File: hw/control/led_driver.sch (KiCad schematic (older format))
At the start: 0 parts

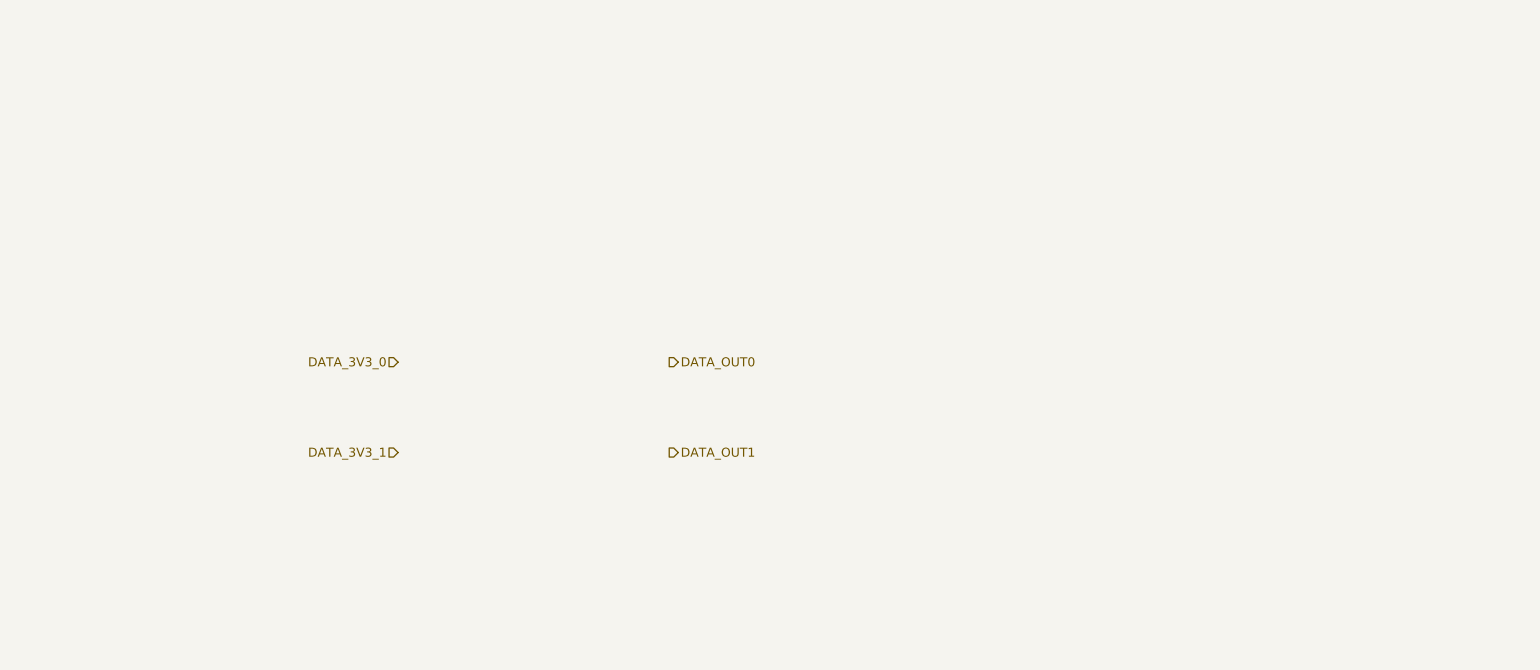
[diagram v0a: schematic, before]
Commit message: [hw] Add LED bus driver
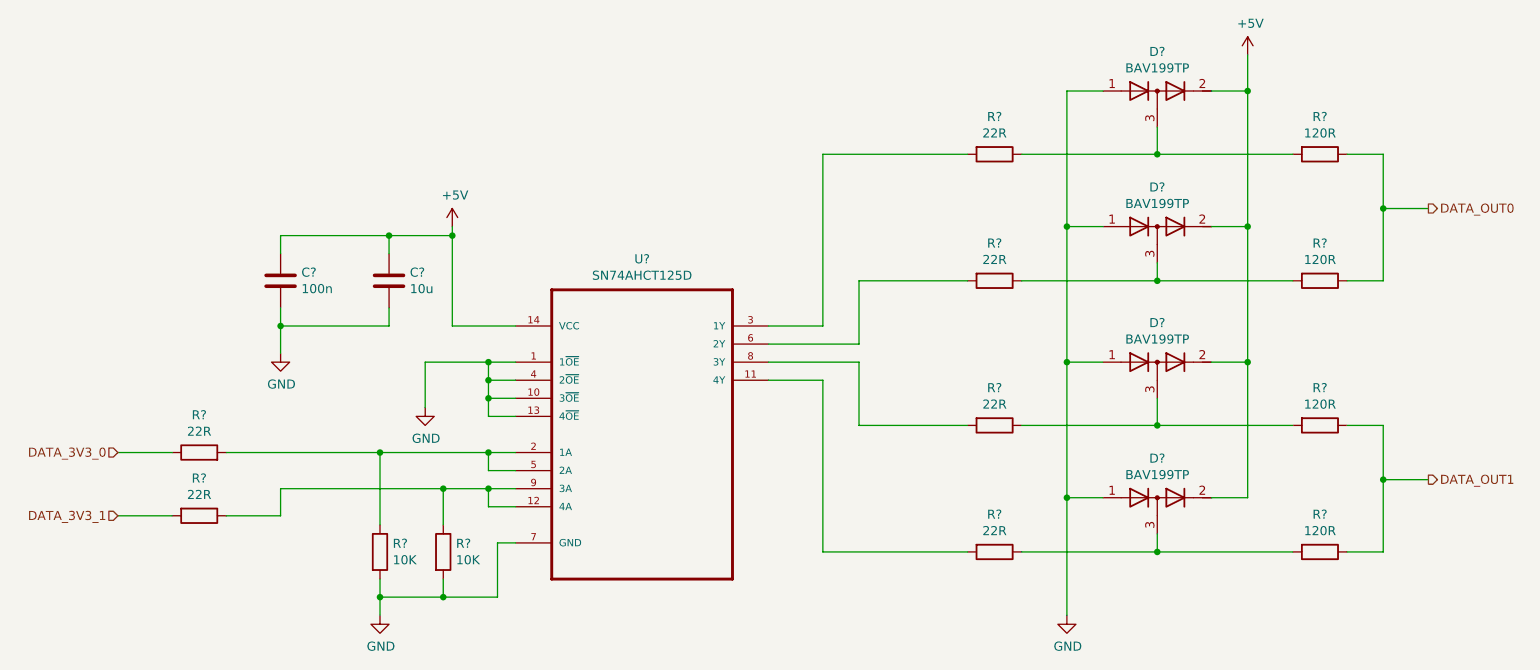
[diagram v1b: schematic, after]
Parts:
- added C?: 10u, symbol Device:C
- added C?: 100n, symbol Device:C
- added D? (x4): BAV199TP, Package_TO_SOT_SMD:SOT-23, symbol my:BAV199TP
- added R? (x2): 10K, symbol Device:R
- added R? (x6): 22R, symbol Device:R
- added R? (x4): 120R, symbol Device:R
- added U?: SN74AHCT125D, SOIC127P600X175-14N, symbol SN74AHCT125D:SN74AHCT125D
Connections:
- net DATA_3V3_0: now also R?.1
- net DATA_3V3_1: now also R?.2
- net DATA_OUT0: now also R?.1, R?.1
- net DATA_OUT1: now also R?.1, R?.1
- new net: R?.2, U?.11 (4Y)
- new net: R?.1, R?.1, U?.12 (4A), U?.9 (3A)
- new net: R?.1, R?.2, U?.2 (1A), U?.5 (2A)
- new net: R?.2, U?.3 (1Y)
- new net: R?.2, U?.6 (2Y)
- new net: R?.2, U?.8 (3Y)
- new net: D?.3 (K3), R?.1, R?.2 (x4)
- new net +5V: C?.1, C?.1, D?.2 (K2), D?.2 (K2), D?.2 (K2), D?.2 (K2), U?.14 (VCC)
- new net GND: C?.2, C?.2, D?.1 (A1), D?.1 (A1), D?.1 (A1), D?.1 (A1), R?.2, R?.2, U?.1 (1~OE), U?.10 (3~OE), U?.13 (4~OE), U?.4 (2~OE), U?.7 (GND)

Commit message: [hw] Add annotations, minor fixes
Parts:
- R707, R708: renamed from R?; value 22R -> 33R
- gave numbers to parts that had none: 17
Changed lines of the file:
@@
 encoding utf-8
 Sheet 7 7
-Title ""
-Date ""
-Rev ""
-Comp ""
-Comment1 ""
+Title "WS2812 Controller"
+Date "2021-09-16"
+Rev "1"
+Comp "Stefan Misik"
+Comment1 "LED Data Driver"
 Comment2 ""
 Comment3 ""
@@
 DATA_OUT1
 $Comp
-L SN74AHCT125D:SN74AHCT125D U?
+L SN74AHCT125D:SN74AHCT125D U701
 U 1 1 6146F060
 P 4850 4300
-F 0 "U?" H 4850 5170 50  0000 C CNN
+F 0 "U701" H 4850 5170 50  0000 C CNN
 F 1 "SN74AHCT125D" H 4850 5079 50  0000 C CNN
 F 2 "SOIC127P600X175-14N" H 4850 4300 50  0001 L BNN
@@
 	4000 4700 4150 4700
 $Comp
-L power:+5V #PWR?
+L power:+5V #PWR0702
 U 1 1 61473D10
 P 3800 3250
-F 0 "#PWR?" H 3800 3100 50  0001 C CNN
+F 0 "#PWR0702" H 3800 3100 50  0001 C CNN
 F 1 "+5V" H 3815 3423 50  0000 C CNN
 F 2 "" H 3800 3250 50  0001 C CNN
@@
 	3800 3800 4150 3800
 $Comp
-L Device:C C?
+L Device:C C702
 U 1 1 6147522C
 P 3450 3550
-F 0 "C?" H 3565 3596 50  0000 L CNN
+F 0 "C702" H 3565 3596 50  0000 L CNN
 F 1 "10u" H 3565 3505 50  0000 L CNN
 F 2 "" H 3488 3400 50  0001 C CNN
@@
 $EndComp
 $Comp
-L Device:C C?
+L Device:C C701
 U 1 1 61475C06
 P 2850 3550
-F 0 "C?" H 2965 3596 50  0000 L CNN
+F 0 "C701" H 2965 3596 50  0000 L CNN
 F 1 "100n" H 2965 3505 50  0000 L CNN
 F 2 "" H 2888 3400 50  0001 C CNN
@@
 	3450 3300 3800 3300
 $Comp
-L power:GND #PWR?
+L power:GND #PWR0703
 U 1 1 61476844
 P 2850 3950
-F 0 "#PWR?" H 2850 3700 50  0001 C CNN
+F 0 "#PWR0703" H 2850 3700 50  0001 C CNN
 F 1 "GND" H 2855 3777 50  0000 C CNN
 F 2 "" H 2850 3950 50  0001 C CNN
@@
 	2850 3800 2850 3700
 $Comp
-L Device:R R?
+L Device:R R710
 U 1 1 6147BD41
 P 3750 5050
-F 0 "R?" H 3820 5096 50  0000 L CNN
+F 0 "R710" H 3820 5096 50  0000 L CNN
 F 1 "10K" H 3820 5005 50  0000 L CNN
 F 2 "" V 3680 5050 50  0001 C CNN
@@
 $EndComp
 $Comp
-L Device:R R?
+L Device:R R709
 U 1 1 6147C52A
 P 3400 5050
-F 0 "R?" H 3470 5096 50  0000 L CNN
+F 0 "R709" H 3470 5096 50  0000 L CNN
 F 1 "10K" H 3470 5005 50  0000 L CNN
 F 2 "" V 3330 5050 50  0001 C CNN
@@
 	3400 4900 3400 4500
 $Comp
-L power:GND #PWR?
+L power:GND #PWR0705
 U 1 1 6147D2D2
 P 3400 5400
-F 0 "#PWR?" H 3400 5150 50  0001 C CNN
+F 0 "#PWR0705" H 3400 5150 50  0001 C CNN
 F 1 "GND" H 3405 5227 50  0000 C CNN
 F 2 "" H 3400 5400 50  0001 C CNN
@@
 Connection ~ 3750 5300
 $Comp
-L power:GND #PWR?
+L power:GND #PWR0704
 U 1 1 614804D8
 P 3650 4250
-F 0 "#PWR?" H 3650 4000 50  0001 C CNN
+F 0 "#PWR0704" H 3650 4000 50  0001 C CNN
 F 1 "GND" H 3655 4077 50  0000 C CNN
 F 2 "" H 3650 4250 50  0001 C CNN
@@
 Connection ~ 4000 4200
 $Comp
-L Device:R R?
+L Device:R R701
 U 1 1 61482CAE
 P 6800 2850
-F 0 "R?" V 6593 2850 50  0000 C CNN
+F 0 "R701" V 6593 2850 50  0000 C CNN
 F 1 "22R" V 6684 2850 50  0000 C CNN
 F 2 "" V 6730 2850 50  0001 C CNN
@@
 $EndComp
 $Comp
-L Device:R R?
+L Device:R R702
 U 1 1 614835EC
 P 8600 2850
-F 0 "R?" V 8393 2850 50  0000 C CNN
+F 0 "R702" V 8393 2850 50  0000 C CNN
 F 1 "120R" V 8484 2850 50  0000 C CNN
 F 2 "" V 8530 2850 50  0001 C CNN
@@
 $EndComp
 $Comp
-L Device:R R?
+L Device:R R703
 U 1 1 61483CB0
 P 6800 3550
-F 0 "R?" V 6593 3550 50  0000 C CNN
+F 0 "R703" V 6593 3550 50  0000 C CNN
 F 1 "22R" V 6684 3550 50  0000 C CNN
 F 2 "" V 6730 3550 50  0001 C CNN
@@
 $EndComp
 $Comp
-L Device:R R?
+L Device:R R704
 U 1 1 61484724
 P 8600 3550
-F 0 "R?" V 8393 3550 50  0000 C CNN
+F 0 "R704" V 8393 3550 50  0000 C CNN
 F 1 "120R" V 8484 3550 50  0000 C CNN
 F 2 "" V 8530 3550 50  0001 C CNN
@@
 $EndComp
 $Comp
-L my:BAV199TP D?
+L my:BAV199TP D701
 U 1 1 6149355D
 P 7700 2500
-F 0 "D?" H 7700 2717 50  0000 C CNN
+F 0 "D701" H 7700 2717 50  0000 C CNN
 F 1 "BAV199TP" H 7700 2626 50  0000 C CNN
 F 2 "Package_TO_SOT_SMD:SOT-23" H 7700 2000 50  0001 C CNN
@@
 $EndComp
 $Comp
-L my:BAV199TP D?
+L my:BAV199TP D702
 U 1 1 61495B2C
 P 7700 3250
-F 0 "D?" H 7700 3467 50  0000 C CNN
+F 0 "D702" H 7700 3467 50  0000 C CNN
 F 1 "BAV199TP" H 7700 3376 50  0000 C CNN
 F 2 "Package_TO_SOT_SMD:SOT-23" H 7700 2750 50  0001 C CNN
@@
 	8950 2850 8750 2850
 $Comp
-L Device:R R?
+L Device:R R705
 U 1 1 614B3F72
 P 6800 4350
-F 0 "R?" V 6593 4350 50  0000 C CNN
+F 0 "R705" V 6593 4350 50  0000 C CNN
 F 1 "22R" V 6684 4350 50  0000 C CNN
 F 2 "" V 6730 4350 50  0001 C CNN
@@
 $EndComp
 $Comp
-L Device:R R?
+L Device:R R706
 U 1 1 614B3F78
 P 8600 4350
-F 0 "R?" V 8393 4350 50  0000 C CNN
+F 0 "R706" V 8393 4350 50  0000 C CNN
 F 1 "120R" V 8484 4350 50  0000 C CNN
 F 2 "" V 8530 4350 50  0001 C CNN
@@
 $EndComp
 $Comp
-L Device:R R?
+L Device:R R711
 U 1 1 614B3F7E
 P 6800 5050
-F 0 "R?" V 6593 5050 50  0000 C CNN
+F 0 "R711" V 6593 5050 50  0000 C CNN
 F 1 "22R" V 6684 5050 50  0000 C CNN
 F 2 "" V 6730 5050 50  0001 C CNN
@@
 $EndComp
 $Comp
-L Device:R R?
+L Device:R R712
 U 1 1 614B3F84
 P 8600 5050
-F 0 "R?" V 8393 5050 50  0000 C CNN
+F 0 "R712" V 8393 5050 50  0000 C CNN
 F 1 "120R" V 8484 5050 50  0000 C CNN
 F 2 "" V 8530 5050 50  0001 C CNN
@@
 $EndComp
 $Comp
-L my:BAV199TP D?
+L my:BAV199TP D703
 U 1 1 614B3F8A
 P 7700 4000
-F 0 "D?" H 7700 4217 50  0000 C CNN
+F 0 "D703" H 7700 4217 50  0000 C CNN
 F 1 "BAV199TP" H 7700 4126 50  0000 C CNN
 F 2 "Package_TO_SOT_SMD:SOT-23" H 7700 3500 50  0001 C CNN
@@
 $EndComp
 $Comp
-L my:BAV199TP D?
+L my:BAV199TP D704
 U 1 1 614B3F90
 P 7700 4750
-F 0 "D?" H 7700 4967 50  0000 C CNN
+F 0 "D704" H 7700 4967 50  0000 C CNN
 F 1 "BAV199TP" H 7700 4876 50  0000 C CNN
 F 2 "Package_TO_SOT_SMD:SOT-23" H 7700 4250 50  0001 C CNN
@@
 	8950 3150 8950 2850
 $Comp
-L Device:R R?
+L Device:R R707
 U 1 1 614BACD3
 P 2400 4500
-F 0 "R?" V 2607 4500 50  0000 C CNN
-F 1 "22R" V 2516 4500 50  0000 C CNN
+F 0 "R707" V 2607 4500 50  0000 C CNN
+F 1 "33R" V 2516 4500 50  0000 C CNN
 F 2 "" V 2330 4500 50  0001 C CNN
 F 3 "~" H 2400 4500 50  0001 C CNN
@@
 $EndComp
 $Comp
-L Device:R R?
+L Device:R R708
 U 1 1 614BBB41
 P 2400 4850
-F 0 "R?" V 2193 4850 50  0000 C CNN
-F 1 "22R" V 2284 4850 50  0000 C CNN
+F 0 "R708" V 2193 4850 50  0000 C CNN
+F 1 "33R" V 2284 4850 50  0000 C CNN
 F 2 "" V 2330 4850 50  0001 C CNN
 F 3 "~" H 2400 4850 50  0001 C CNN
@@
 	6050 3550 6650 3550
 $Comp
-L power:+5V #PWR?
+L power:+5V #PWR0701
 U 1 1 614ECF7C
 P 8200 2300
-F 0 "#PWR?" H 8200 2150 50  0001 C CNN
+F 0 "#PWR0701" H 8200 2150 50  0001 C CNN
 F 1 "+5V" H 8215 2473 50  0000 C CNN
 F 2 "" H 8200 2300 50  0001 C CNN
@@
 Connection ~ 8200 4000
 $Comp
-L power:GND #PWR?
+L power:GND #PWR0706
 U 1 1 614F54C4
 P 7200 5400
-F 0 "#PWR?" H 7200 5150 50  0001 C CNN
+F 0 "#PWR0706" H 7200 5150 50  0001 C CNN
 F 1 "GND" H 7205 5227 50  0000 C CNN
 F 2 "" H 7200 5400 50  0001 C CNN

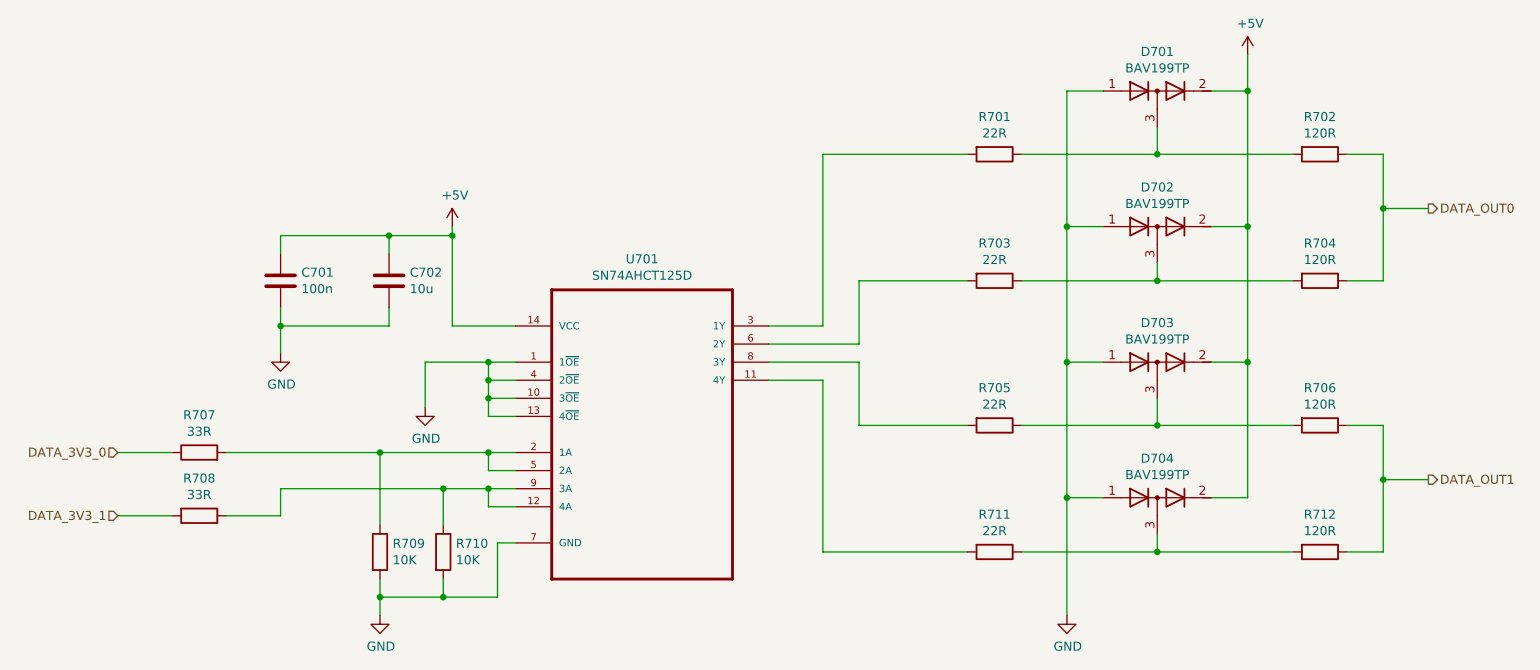
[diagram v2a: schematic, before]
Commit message: [hw] Add LED driver output sheets
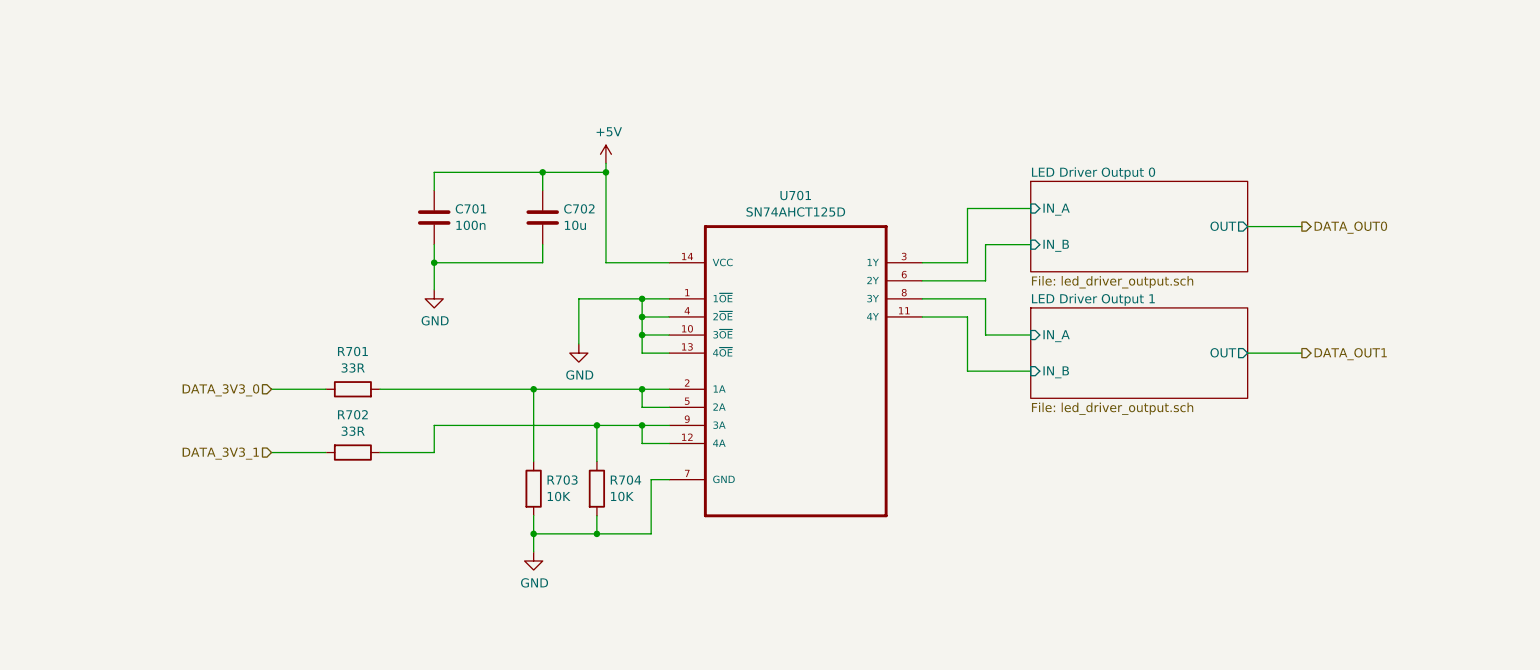
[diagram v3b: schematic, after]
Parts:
- removed D701, D702, D703, D704: BAV199TP, Package_TO_SOT_SMD:SOT-23, symbol my:BAV199TP
- removed R701, R703, R705, R711: 22R, symbol Device:R
- removed R702, R704, R706, R712: 120R, symbol Device:R
- renumbered R707 to R701, R708 to R702, R709 to R703, R710 to R704
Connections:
- net LED Driver Output 1/IN_B: now reaches U701.11 (4Y)
- net LED Driver Output 0/IN_A: now reaches U701.3 (1Y)
- net LED Driver Output 0/IN_B: now reaches U701.6 (2Y)
- net LED Driver Output 1/IN_A: now reaches U701.8 (3Y)
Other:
- moved on the sheet: C701, C702, R701, R702, R703, R704, U701

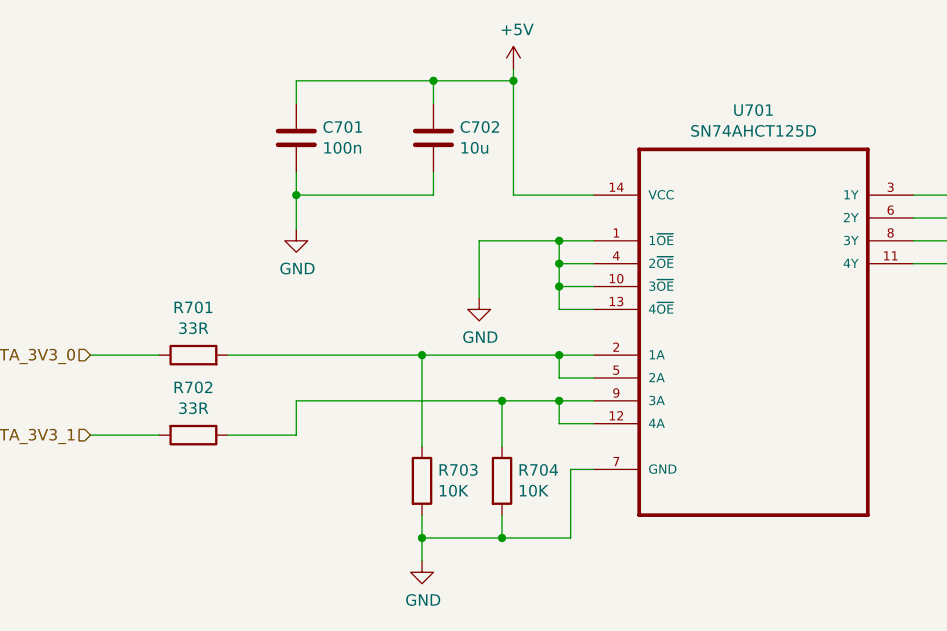
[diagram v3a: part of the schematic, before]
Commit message: [hw] Add some more peripherals
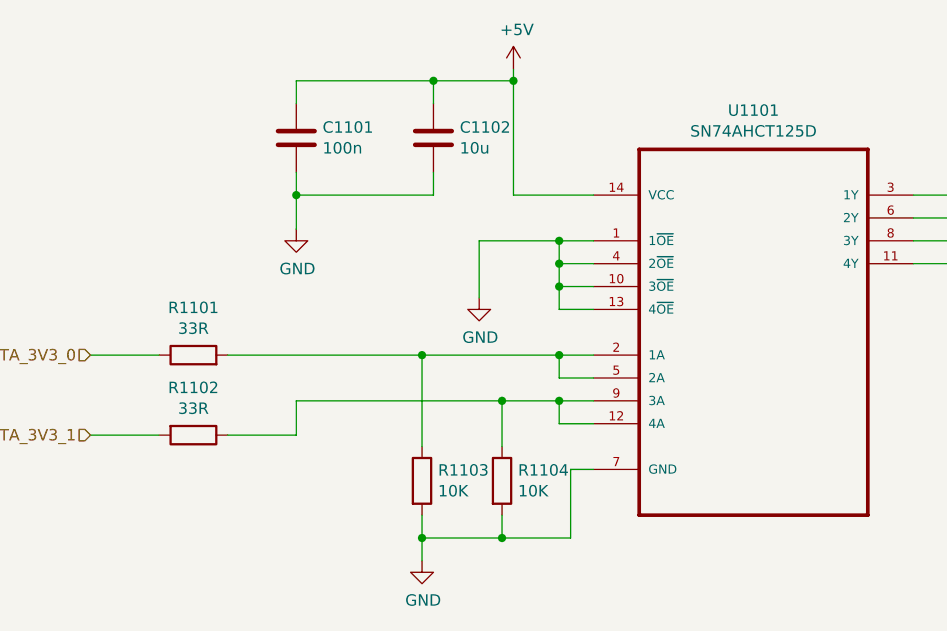
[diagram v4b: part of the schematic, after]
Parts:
- renumbered C701 to C1101, C702 to C1102, R701 to R1101, R702 to R1102, R703 to R1103, R704 to R1104, U701 to U1101
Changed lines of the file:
@@
 $Descr A4 11693 8268
 encoding utf-8
-Sheet 7 9
+Sheet 7 13
 Title "WS2812 Controller"
-Date "2021-09-21"
+Date "2021-10-10"
 Rev "1"
 Comp "Stefan Misik"
@@
 DATA_OUT1
 $Comp
-L SN74AHCT125D:SN74AHCT125D U701
+L SN74AHCT125D:SN74AHCT125D U1101
 U 1 1 6146F060
 P 5700 3950
-F 0 "U701" H 5700 4820 50  0000 C CNN
+F 0 "U1101" H 5700 4820 50  0000 C CNN
 F 1 "SN74AHCT125D" H 5700 4729 50  0000 C CNN
 F 2 "SOIC127P600X175-14N" H 5700 3950 50  0001 L BNN
@@
 	4850 4350 5000 4350
 $Comp
-L power:+5V #PWR0704
+L power:+5V #PWR01101
 U 1 1 61473D10
 P 4650 2900
-F 0 "#PWR0704" H 4650 2750 50  0001 C CNN
+F 0 "#PWR01101" H 4650 2750 50  0001 C CNN
 F 1 "+5V" H 4665 3073 50  0000 C CNN
 F 2 "" H 4650 2900 50  0001 C CNN
@@
 	4650 3450 5000 3450
 $Comp
-L Device:C C702
+L Device:C C1102
 U 1 1 6147522C
 P 4300 3200
-F 0 "C702" H 4415 3246 50  0000 L CNN
+F 0 "C1102" H 4415 3246 50  0000 L CNN
 F 1 "10u" H 4415 3155 50  0000 L CNN
 F 2 "" H 4338 3050 50  0001 C CNN
@@
 $EndComp
 $Comp
-L Device:C C701
+L Device:C C1101
 U 1 1 61475C06
 P 3700 3200
-F 0 "C701" H 3815 3246 50  0000 L CNN
+F 0 "C1101" H 3815 3246 50  0000 L CNN
 F 1 "100n" H 3815 3155 50  0000 L CNN
 F 2 "" H 3738 3050 50  0001 C CNN
@@
 	4300 2950 4650 2950
 $Comp
-L power:GND #PWR0701
+L power:GND #PWR01102
 U 1 1 61476844
 P 3700 3600
-F 0 "#PWR0701" H 3700 3350 50  0001 C CNN
+F 0 "#PWR01102" H 3700 3350 50  0001 C CNN
 F 1 "GND" H 3705 3427 50  0000 C CNN
 F 2 "" H 3700 3600 50  0001 C CNN
@@
 	3700 3450 3700 3350
 $Comp
-L Device:R R704
+L Device:R R1104
 U 1 1 6147BD41
 P 4600 4700
-F 0 "R704" H 4670 4746 50  0000 L CNN
+F 0 "R1104" H 4670 4746 50  0000 L CNN
 F 1 "10K" H 4670 4655 50  0000 L CNN
 F 2 "" V 4530 4700 50  0001 C CNN
@@
 $EndComp
 $Comp
-L Device:R R703
+L Device:R R1103
 U 1 1 6147C52A
 P 4250 4700
-F 0 "R703" H 4320 4746 50  0000 L CNN
+F 0 "R1103" H 4320 4746 50  0000 L CNN
 F 1 "10K" H 4320 4655 50  0000 L CNN
 F 2 "" V 4180 4700 50  0001 C CNN
@@
 	4250 4550 4250 4150
 $Comp
-L power:GND #PWR0702
+L power:GND #PWR01104
 U 1 1 6147D2D2
 P 4250 5050
-F 0 "#PWR0702" H 4250 4800 50  0001 C CNN
+F 0 "#PWR01104" H 4250 4800 50  0001 C CNN
 F 1 "GND" H 4255 4877 50  0000 C CNN
 F 2 "" H 4250 5050 50  0001 C CNN
@@
 Connection ~ 4600 4950
 $Comp
-L power:GND #PWR0703
+L power:GND #PWR01103
 U 1 1 614804D8
 P 4500 3900
-F 0 "#PWR0703" H 4500 3650 50  0001 C CNN
+F 0 "#PWR01103" H 4500 3650 50  0001 C CNN
 F 1 "GND" H 4505 3727 50  0000 C CNN
 F 2 "" H 4500 3900 50  0001 C CNN
@@
 Connection ~ 4850 3850
 $Comp
-L Device:R R701
+L Device:R R1101
 U 1 1 614BACD3
 P 3250 4150
-F 0 "R701" V 3457 4150 50  0000 C CNN
+F 0 "R1101" V 3457 4150 50  0000 C CNN
 F 1 "33R" V 3366 4150 50  0000 C CNN
 F 2 "" V 3180 4150 50  0001 C CNN
@@
 $EndComp
 $Comp
-L Device:R R702
+L Device:R R1102
 U 1 1 614BBB41
 P 3250 4500
-F 0 "R702" V 3043 4500 50  0000 C CNN
+F 0 "R1102" V 3043 4500 50  0000 C CNN
 F 1 "33R" V 3134 4500 50  0000 C CNN
 F 2 "" V 3180 4500 50  0001 C CNN
